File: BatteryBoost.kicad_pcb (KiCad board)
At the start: 2 copper layers, 80 x 40 mm, 44 parts, among them J1 Mounting Hole, J2 Mounting Hole, J3 Mounting Hole, J4 Mounting Hole, J5 USB_B_Micro, J6 Battery, J7 Output, Q1 -40V 7.5A 2.5V @ 250uA 40mΩ @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, Q2 -40V 7.5A 40mΩ @ 6A, Q4 20V 7.5A 24mΩ @ 2.5Vgs, SW1 SW_SPDT, U1 SP34063AEN, U2 TP4056, U3 AP9101CK6

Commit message: Update routing
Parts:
- turned R8 to 90 degrees
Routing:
- net SMPS_Pwr: track 92.4 -> 62.7 mm, vias 15 -> 14
- net Net-(L1-Pad2): track 25.1 -> 0.35 mm, vias 0 -> 7
- added copper zone on B.Cu, net Net-(L1-Pad2)

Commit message: finalize bottom artwork
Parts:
- added G***: LOGO, BatteryBoost:B_Artwork, B.Cu at (40.0, 20.0)
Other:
- board text added: "JLCJLCJLCJLC"

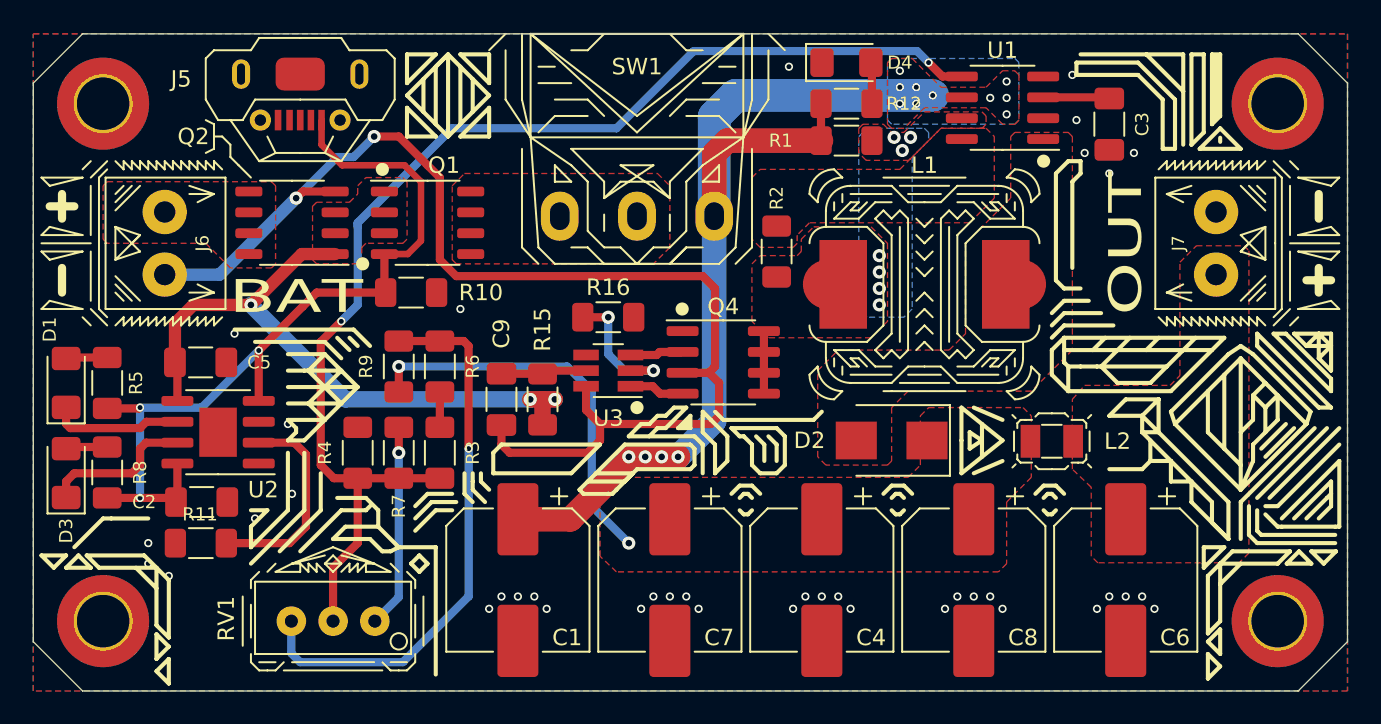
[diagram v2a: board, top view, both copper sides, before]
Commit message: Update part info for sourcing issues
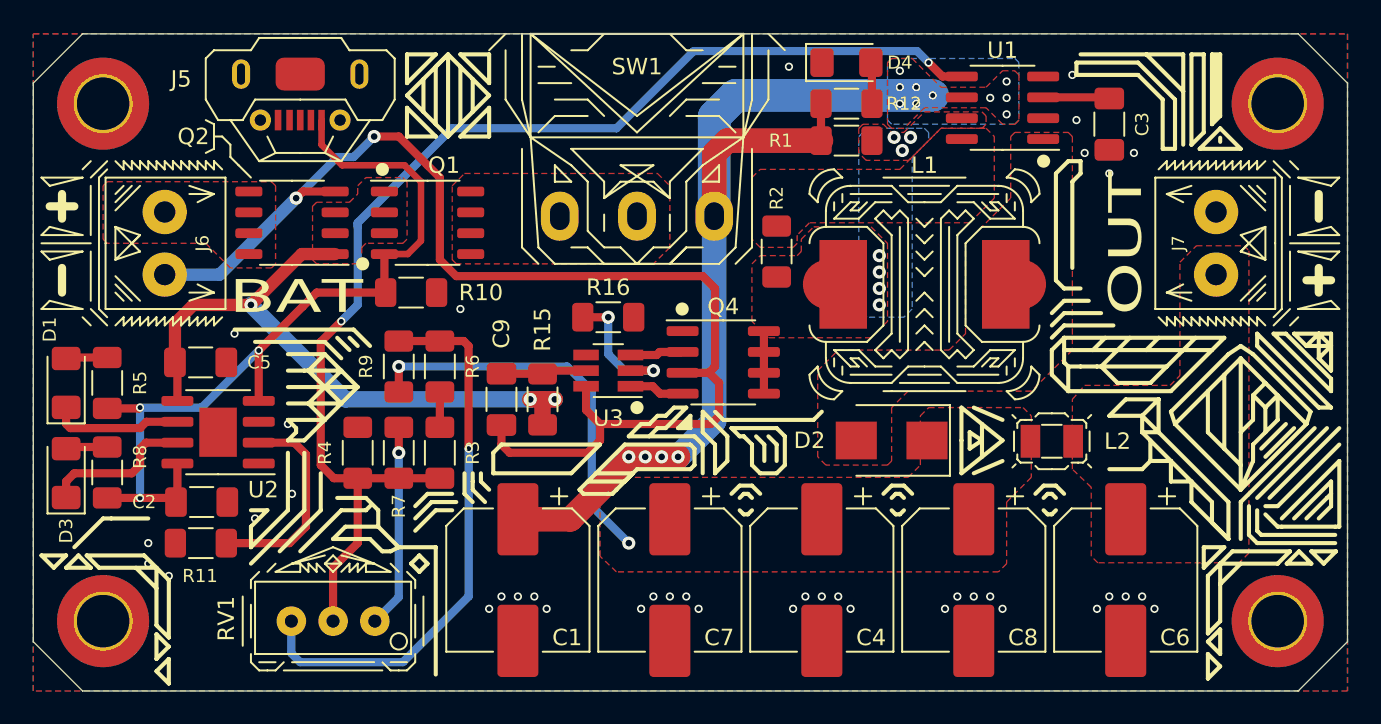
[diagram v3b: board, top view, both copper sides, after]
